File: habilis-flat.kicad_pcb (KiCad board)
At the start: 2 copper layers, 167.6 x 168.5 mm, 73 parts, among them J1 AudioJack4, SW1 MX, SW10 MX, SW11 MX, SW12 MX, SW13 MX, SW14 MX, SW15 MX, SW16 MX, SW17 MX, SW18 MX, SW19 MX, SW2 MX, SW20 MX, SW21 MX, SW22 MX, SW23 MX, SW24 MX, SW25 MX, SW26 MX, SW27 MX, SW28 MX, SW29 MX, SW3 MX, SW30 MX, SW31 MX, SW32 MX, SW33 MX, SW34 MX, SW35 MX, SW4 MX, SW5 MX, SW6 MX, SW7 MX, SW8 MX, SW9 MX, U1 ProMicro

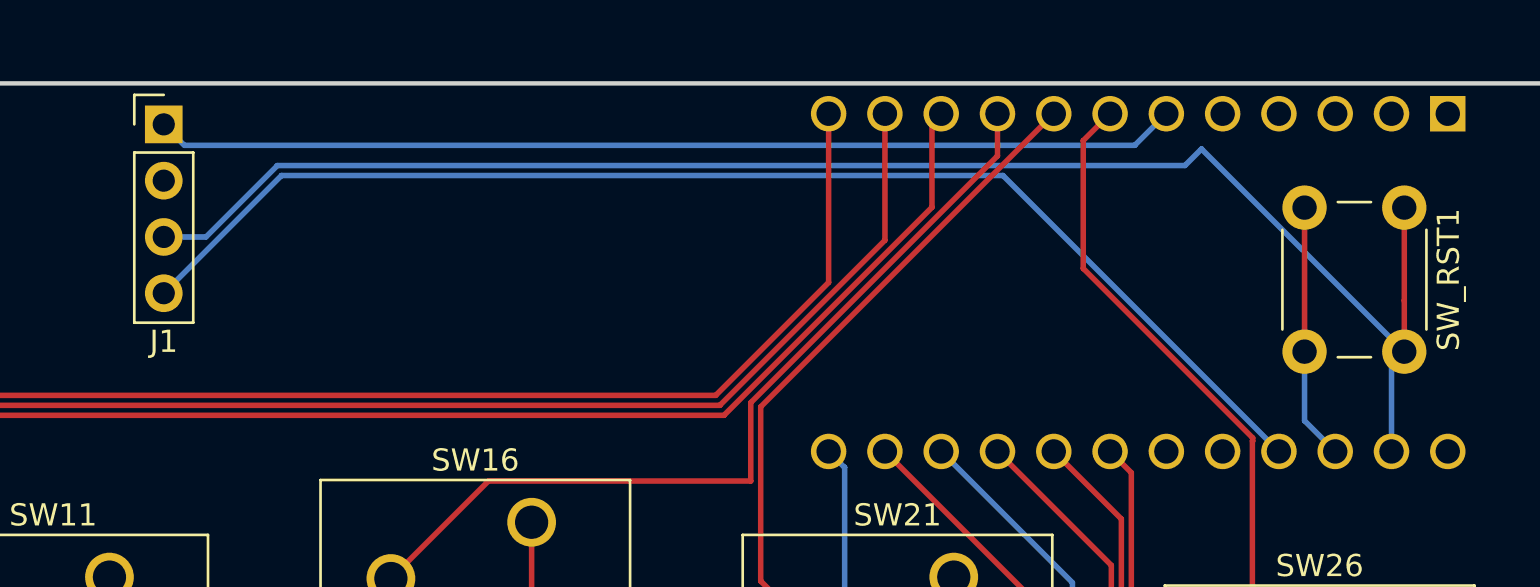
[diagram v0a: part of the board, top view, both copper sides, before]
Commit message: Merge R1 and R2 of the TRRS
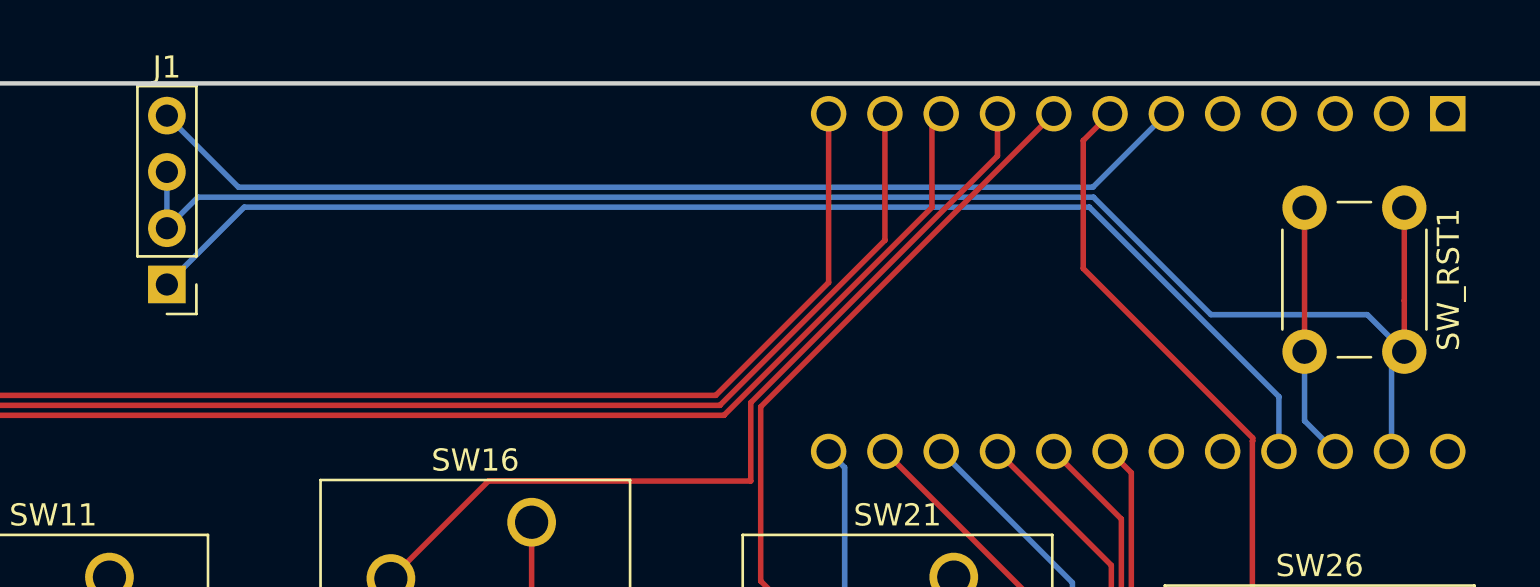
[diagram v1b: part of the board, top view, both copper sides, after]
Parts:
- moved J1 7.23 mm to (83.7, 11.2), turned to 180 degrees
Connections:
- J1 pad R1: Net-(U1-VCC) -> Net-(J1-PadR1)
- J1 pad R2: Net-(U1-SCL) -> Net-(J1-PadR1)
- J1 pad S: unconnected-(J1-PadS) -> Net-(U1-SCL)
- J1 pad T: Net-(J1-PadT) -> Net-(U1-VCC)
- SW_RST1 pad 1: Net-(J1-PadT) -> Net-(J1-PadR1)
- U1 pad 23: Net-(J1-PadT) -> Net-(J1-PadR1)
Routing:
- net Net-(J1-PadR1): track 0.00 -> 73.1 mm
- net Net-(J1-PadT): track 72.7 -> 0.00 mm
- net Net-(U1-SCL): track 46.2 -> 47.8 mm

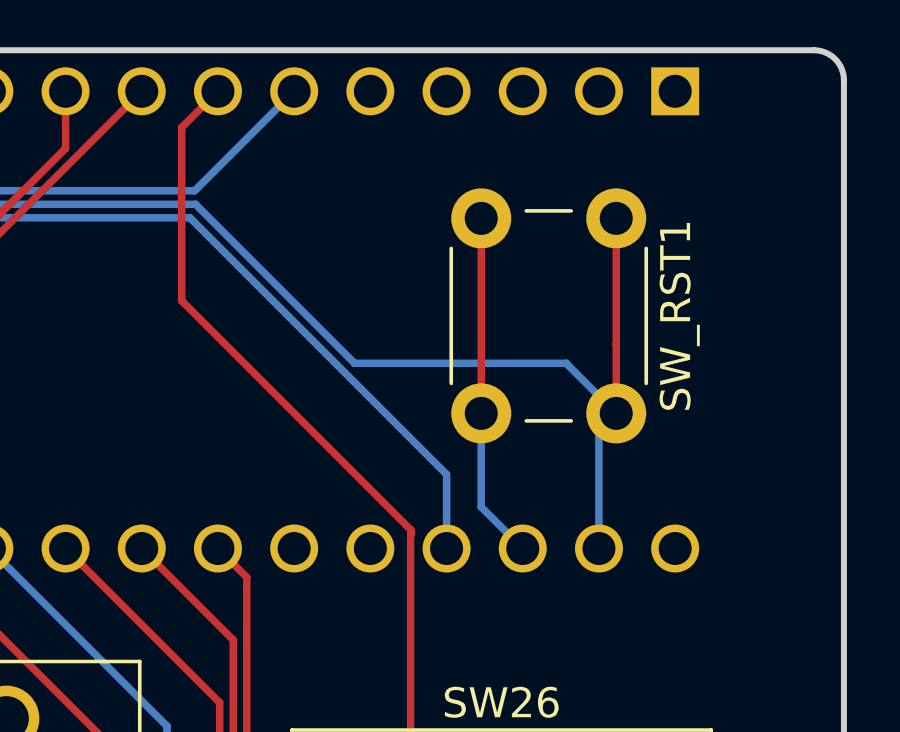
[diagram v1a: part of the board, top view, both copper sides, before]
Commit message: Put reset switch on the opposite side
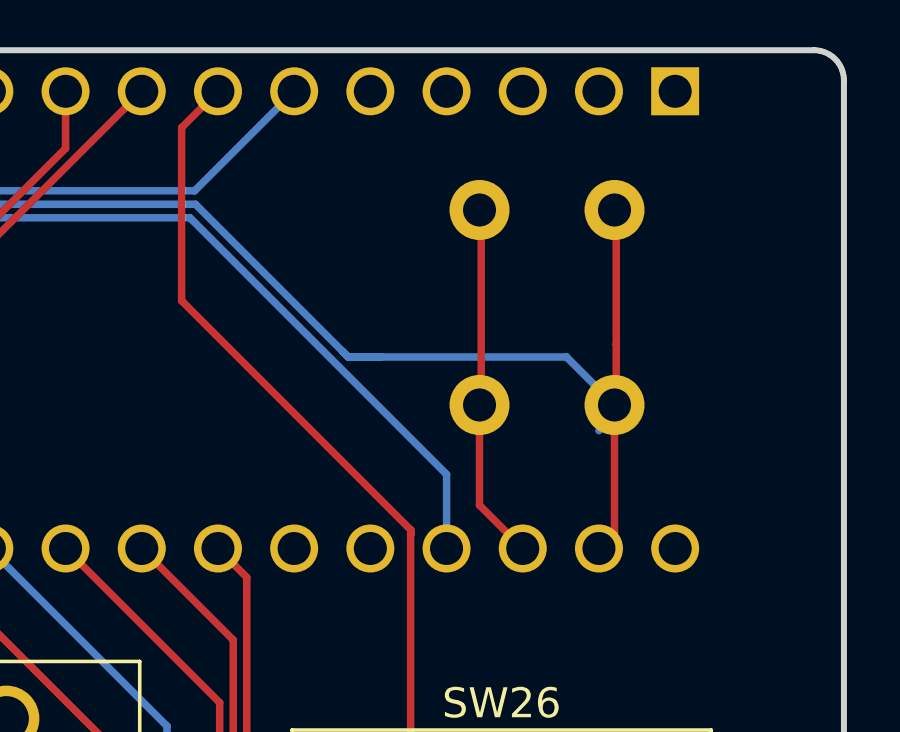
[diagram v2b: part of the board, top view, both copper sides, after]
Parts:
- SW_RST1: moved to B.Cu
- moved SW_RST1 4.57 mm to (135.0, 7.46)
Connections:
- SW_RST1 pad 1: Net-(J1-PadR1) -> Net-(U1-RST)
- SW_RST1 pad 2: Net-(U1-RST) -> Net-(J1-PadR1)
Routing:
- net Net-(J1-PadR1): track 73.1 -> 75.4 mm

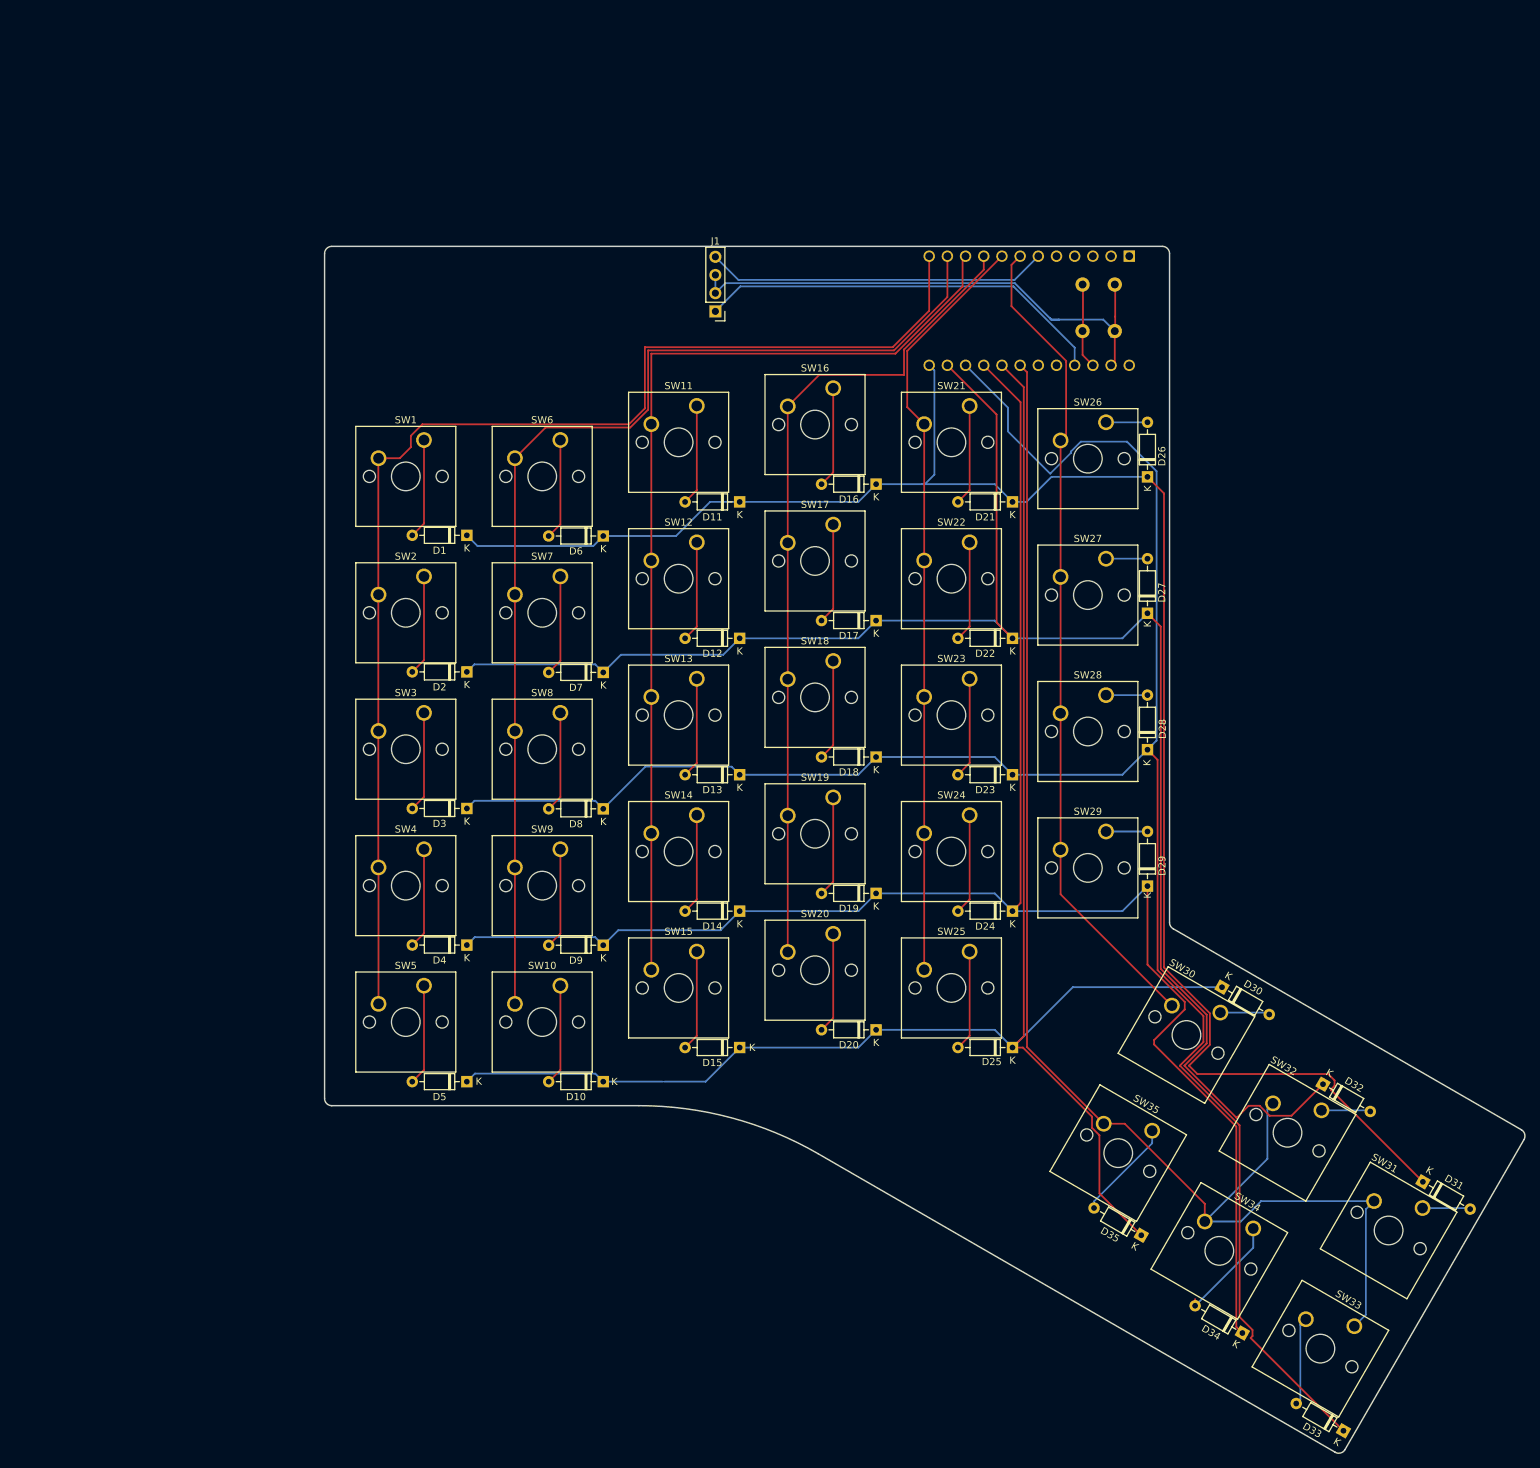
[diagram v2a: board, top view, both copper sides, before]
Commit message: Replace MX footprint with reversible version
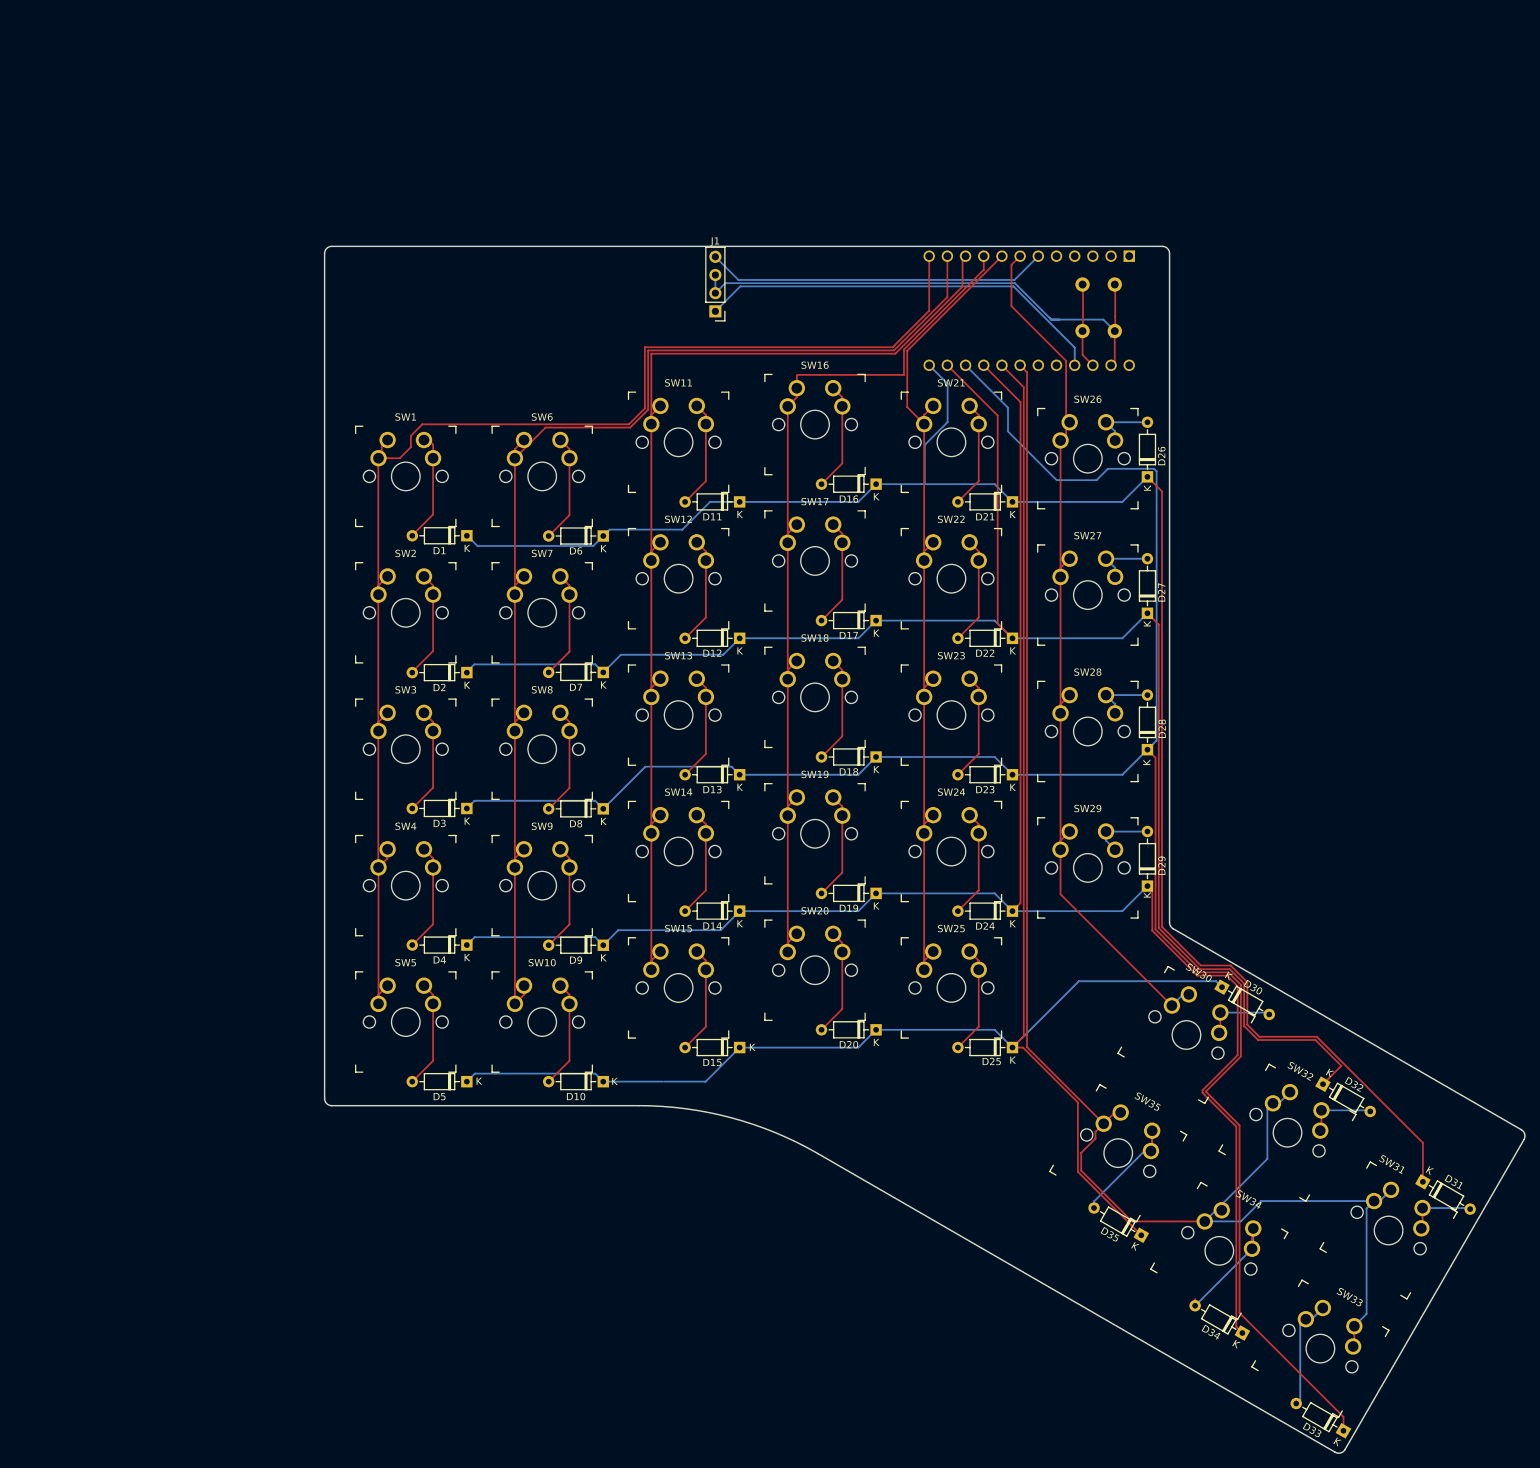
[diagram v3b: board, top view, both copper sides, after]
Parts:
- SW1, SW10, SW11, SW12, SW13, SW14, SW15, SW16, SW17, SW18, SW19, SW2, SW20, SW21, SW22, SW23, SW24, SW25, SW26, SW27, SW28, SW29, SW3, SW30, SW31, SW32, SW33, SW34, SW35, SW4, SW5, SW6, SW7, SW8, SW9: footprint Button_Switch_Keyboard:SW_Cherry_MX_1.00u_PCB -> project-components:SW_MX_reversible_decentered
- moved D2 0.10 mm to (49.0, 61.7)
- moved D1 0.06 mm to (49.0, 42.5)
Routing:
- net Net-(U1-F6): track 196.9 -> 215.7 mm
- net Net-(U1-E6): track 137.8 -> 153.3 mm
- net Net-(U1-B4): track 156.5 -> 171.9 mm
- net Net-(U1-C6): track 106.1 -> 121.4 mm
- net Net-(U1-B5): track 175.8 -> 191.0 mm
- net Net-(U1-D7): track 115.4 -> 129.5 mm
- net Net-(U1-D4): track 115.1 -> 127.7 mm
- net Net-(D12-K): track 236.7 -> 228.5 mm
- net Net-(D1-K): track 247.3 -> 242.4 mm
- net Net-(D28-A): track 5.78 -> 8.85 mm
- net Net-(D29-A): track 5.78 -> 8.85 mm
- net Net-(D27-A): track 5.78 -> 8.85 mm
- net Net-(D26-A): track 5.78 -> 8.85 mm
- net Net-(D33-A): track 12.4 -> 15.4 mm
- net Net-(D14-K): track 251.7 -> 254.7 mm
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
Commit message: Cleanup some tracks
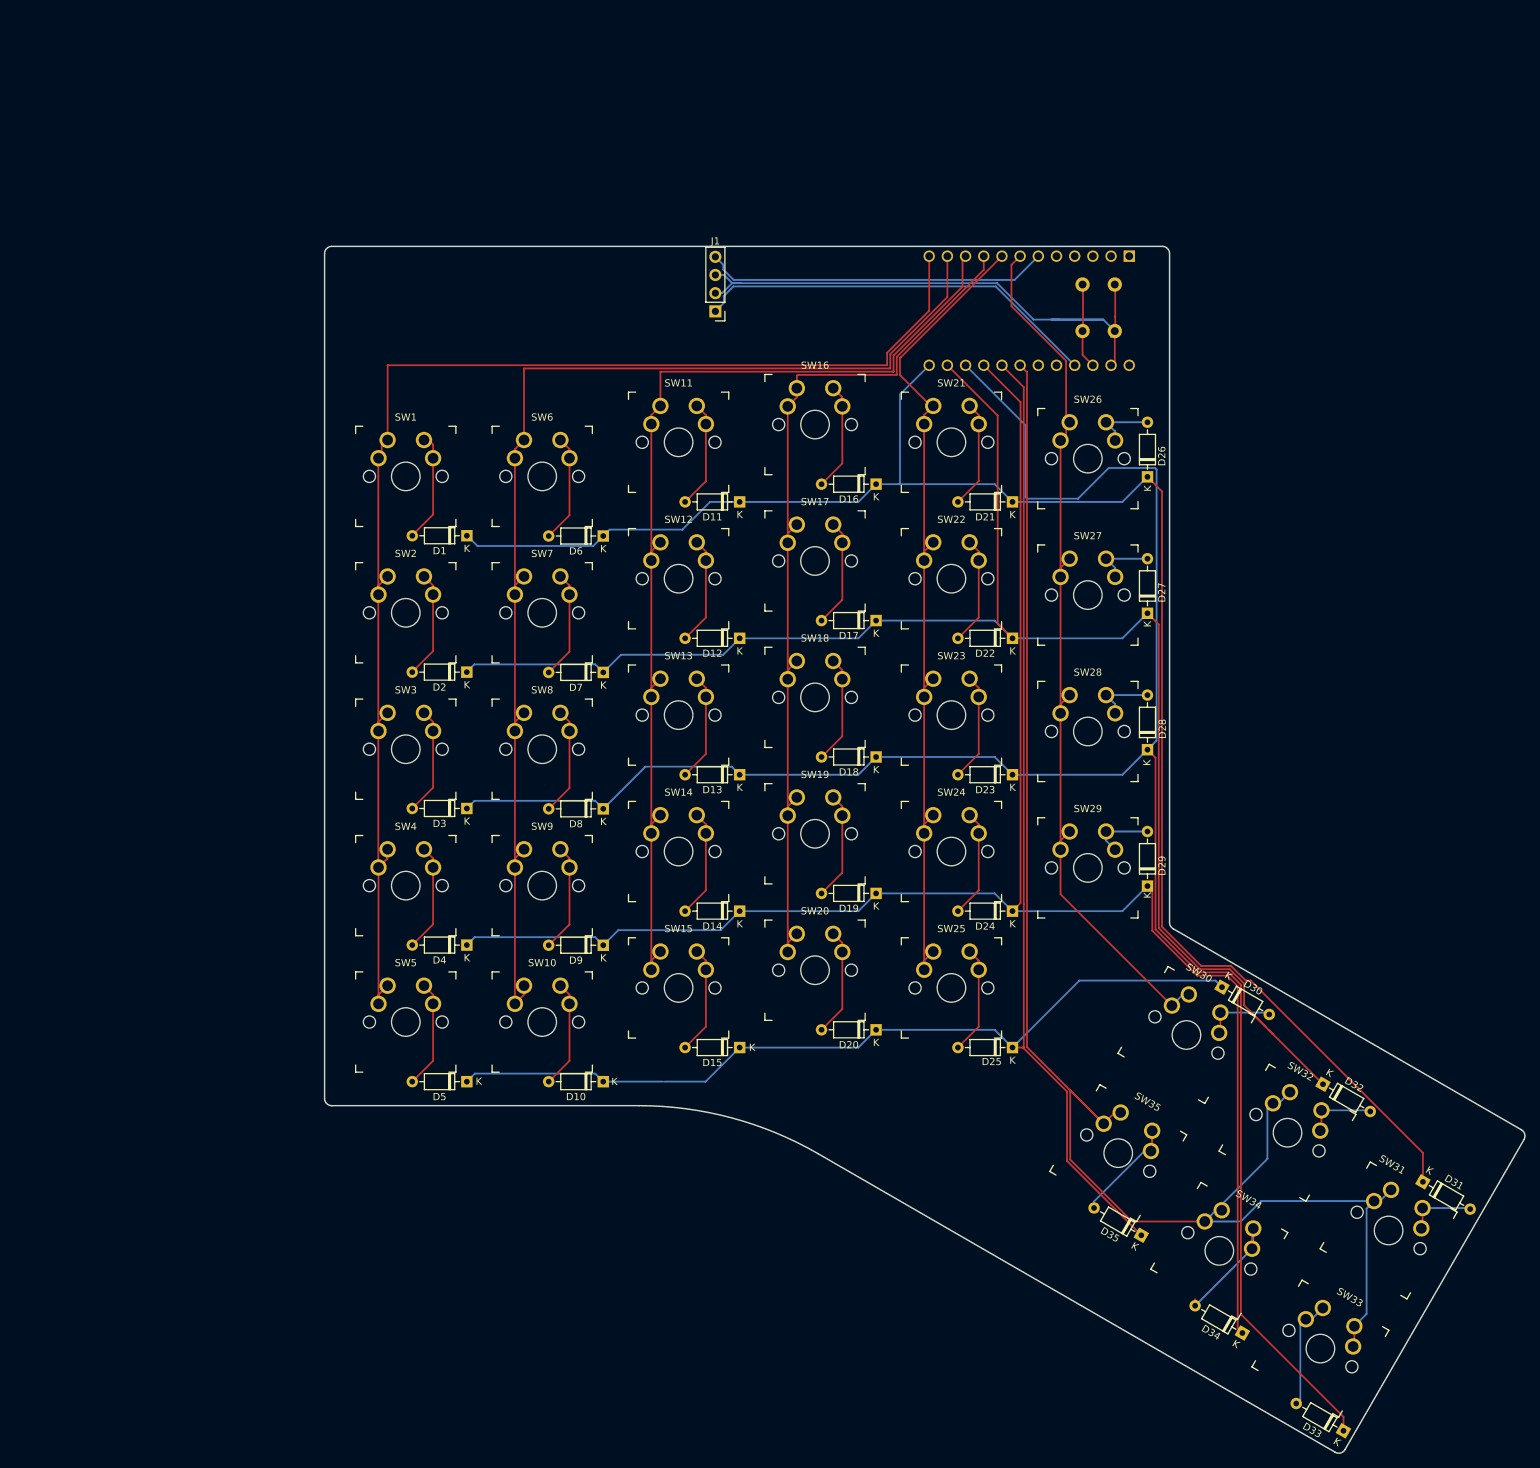
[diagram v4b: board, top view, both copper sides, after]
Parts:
- moved D2 0.07 mm to (49.0, 61.6)
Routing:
- net Net-(U1-F6): track 215.7 -> 225.3 mm
- net Net-(J1-PadR1): track 75.4 -> 83.9 mm
- net Net-(D1-K): track 242.4 -> 237.6 mm
- net Net-(D14-K): track 254.7 -> 250.6 mm
- net Net-(U1-E6): track 153.3 -> 149.3 mm
- net Net-(D12-K): track 228.5 -> 225.6 mm
- net Net-(D13-K): track 290.8 -> 293.1 mm
- net Net-(U1-B5): track 191.0 -> 189.9 mm
- net Net-(U1-C6): track 121.4 -> 120.5 mm
- net Net-(U1-VCC): track 57.6 -> 56.8 mm
- net Net-(U1-D7): track 129.5 -> 128.9 mm
